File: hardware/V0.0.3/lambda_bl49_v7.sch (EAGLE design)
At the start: 58 parts, among them IC10 MCP2551-E/SN, IC3 LMV321IDBVR, IC4 TLS115B0EJXUMA1, IC6 TLE4270-2D, IC9 CJ125_32, Q3 ABM3-16.000MHZ-D2Y-T

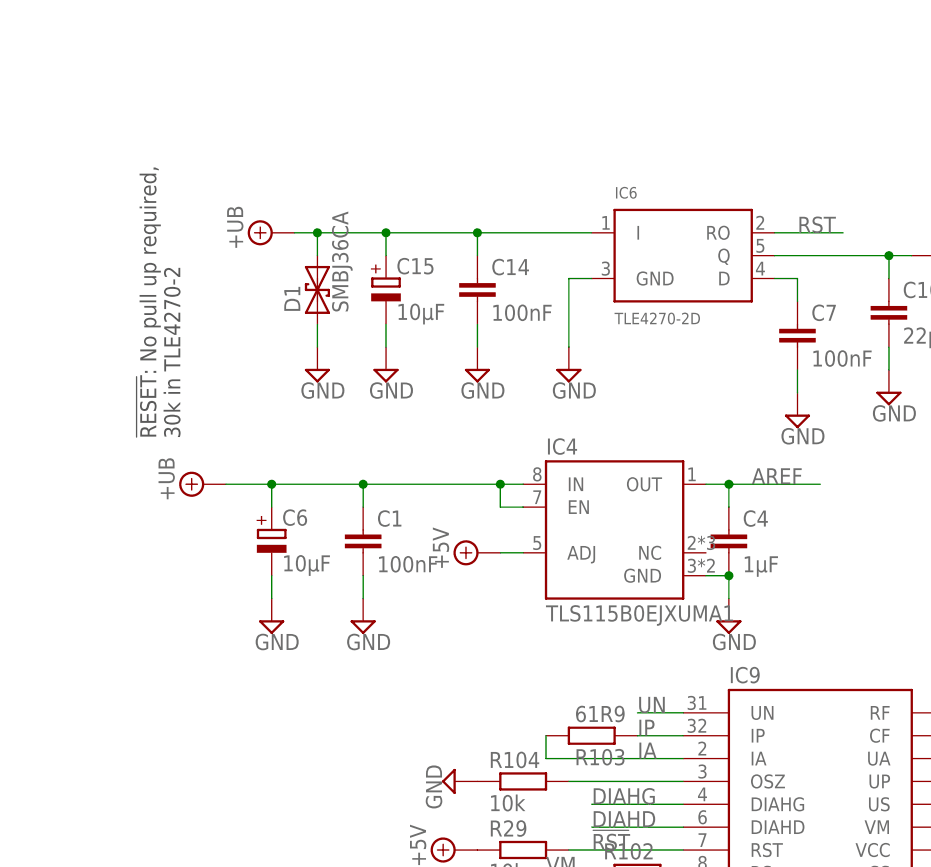
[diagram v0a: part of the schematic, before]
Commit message: tls115 replaced by ti ref5050
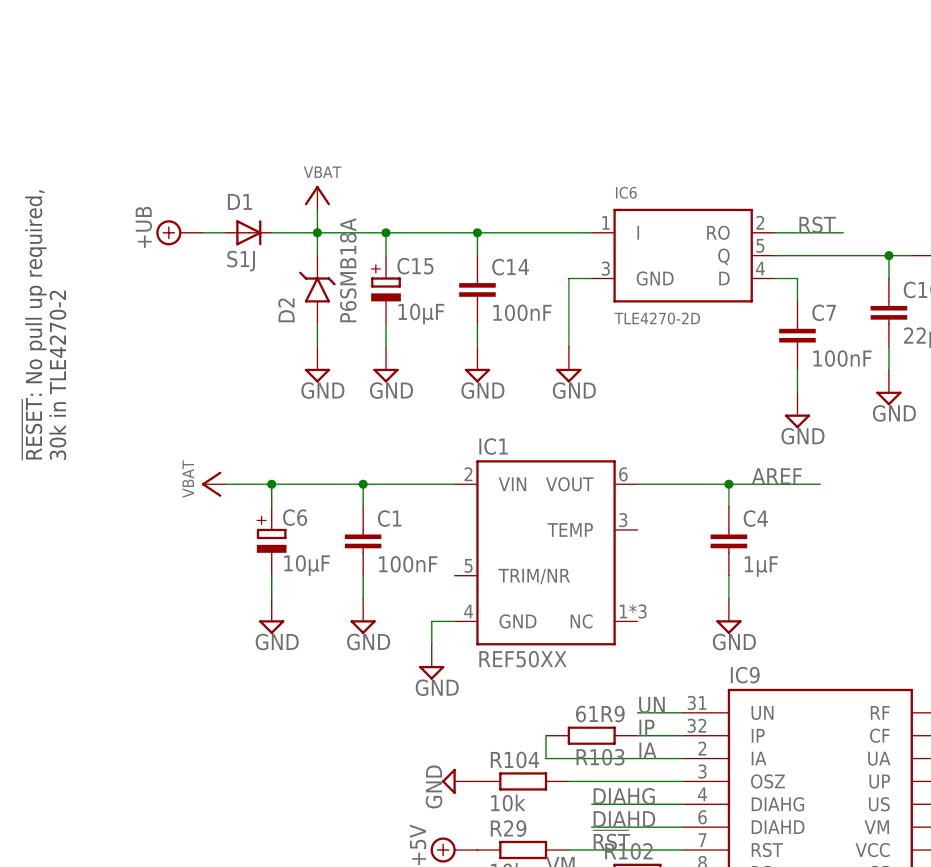
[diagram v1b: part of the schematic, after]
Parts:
- removed IC4: TLS115B0EJXUMA1, Heinrich:TLS115B0EJXUMA1
- added D2: P6SMB18A, Heinrich:P6SMBXXASMB
- added IC1: REF50XX, Heinrich:REF50XX
- D1: value SMBJ36CA -> S1J; device Heinrich:P6SMBXXCA -> Heinrich:DIODESMA
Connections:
- new net VBAT: C1.1, C14.1, C15.+, C6.+, D1.C, D2.C, IC1.VIN, IC6.I
- net +5V: no longer IC4.ADJ
- net +UB: now also D1.A; no longer C1.1, C14.1, C15.+, C6.+, D1.2, IC4.EN, IC4.IN, IC6.I
- net AREF: now also IC1.VOUT; no longer IC4.OUT
- net GND: now also D2.A, IC1.GND; no longer D1.1, IC4.GND
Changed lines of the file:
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@@
 <part name="SUPPLY11" library="supply2" deviceset="+12V" device=""/>
 <part name="SUPPLY6" library="supply2" deviceset="+12V" device=""/>
-<part name="IC4" library="Heinrich" deviceset="TLS115B0EJXUMA1" device=""/>
 <part name="U$12" library="supply2@1" deviceset="GND" device=""/>
 <part name="C4" library="rcl@1" deviceset="C-EU" device="C0603" value="1µF"/>
@@
 <part name="U$13" library="supply2@1" deviceset="GND" device=""/>
 <part name="U$14" library="supply2@1" deviceset="GND" device=""/>
-<part name="D1" library="Heinrich" deviceset="P6SMBXXCA" device="" value="SMBJ36CA"/>
 <part name="C14" library="rcl@1" deviceset="C-EU" device="C0603" value="100nF"/>
 <part name="C15" library="rcl@1" deviceset="CPOL-EU" device="D" value="10µF"/>
@@
 <part name="SUPPLY16" library="supply2@1" deviceset="GND" device=""/>
 <part name="C8" library="rcl@1" deviceset="C-EU" device="C0603" value="100nF"/>
-<part name="SUPPLY17" library="supply2@1" deviceset="+UB" device=""/>
 <part name="SUPPLY18" library="supply2@1" deviceset="GND" device=""/>
 <part name="SUPPLY20" library="supply2@1" deviceset="GND" device=""/>
@@
 <part name="SUPPLY19" library="supply2@1" deviceset="GND" device=""/>
 <part name="SUPPLY22" library="supply2@1" deviceset="GND" device=""/>
-<part name="SUPPLY3" library="supply2@1" deviceset="+5V" device=""/>
+<part name="IC1" library="Heinrich" deviceset="REF50XX" device=""/>
+<part name="SUPPLY3" library="supply2@1" deviceset="GND" device=""/>
+<part name="D2" library="Heinrich" deviceset="P6SMBXXA" device="SMB" value="P6SMB18A"/>
+<part name="D1" library="Heinrich" deviceset="DIODE" device="SMA" value="S1J"/>
+<part name="U$4" library="microbuilder" deviceset="VBAT" device=""/>
+<part name="U$5" library="microbuilder" deviceset="VBAT" device=""/>
 </parts>
 <sheets>
@@
 <text x="227.076" y="167.64" size="1.778" layer="95">1.</text>
 <text x="227.076" y="154.94" size="1.778" layer="95">6.</text>
-<text x="10.16" y="144.78" size="1.778" layer="97" rot="R90">!RESET!: No pull up required,
+<text x="-2.54" y="142.24" size="1.778" layer="97" rot="R90">!RESET!: No pull up required,
 30k in TLE4270-2</text>
 </plain>
@@
 <instance part="LED1" gate="G$1" x="114.3" y="154.94"/>
 <instance part="SUPPLY1" gate="+5V" x="114.3" y="162.56"/>
-<instance part="SUPPLY5" gate="G$1" x="20.32" y="167.64" rot="R90"/>
+<instance part="SUPPLY5" gate="G$1" x="10.16" y="167.64" rot="R90"/>
 <instance part="IC3" gate="G$1" x="139.7" y="33.02"/>
 <instance part="R5" gate="G$1" x="119.38" y="35.56" rot="R180"/>
@@
 <instance part="SUPPLY11" gate="+12V" x="182.88" y="162.56" rot="R270"/>
 <instance part="SUPPLY6" gate="+12V" x="91.44" y="38.1"/>
-<instance part="IC4" gate="G$1" x="58.42" y="134.62"/>
 <instance part="U$12" gate="GND" x="71.12" y="124.46"/>
 <instance part="C4" gate="G$1" x="71.12" y="134.62"/>
@@
 <instance part="U$13" gate="GND" x="20.32" y="124.46"/>
 <instance part="U$14" gate="GND" x="30.48" y="124.46"/>
-<instance part="D1" gate="G$1" x="25.4" y="160.02" rot="R90"/>
 <instance part="C14" gate="G$1" x="43.18" y="162.56"/>
 <instance part="C15" gate="G$1" x="33.02" y="162.56"/>
@@
 <instance part="SUPPLY16" gate="GND" x="53.34" y="152.4"/>
 <instance part="C8" gate="G$1" x="55.88" y="78.74"/>
-<instance part="SUPPLY17" gate="G$1" x="12.7" y="139.7" rot="R90"/>
 <instance part="SUPPLY18" gate="GND" x="226.06" y="99.06"/>
 <instance part="SUPPLY20" gate="GND" x="114.3" y="134.62"/>
@@
 <instance part="SUPPLY19" gate="GND" x="208.28" y="58.42"/>
 <instance part="SUPPLY22" gate="GND" x="218.44" y="58.42"/>
-<instance part="SUPPLY3" gate="+5V" x="43.18" y="132.08" rot="R90"/>
+<instance part="IC1" gate="G$1" x="50.8" y="132.08"/>
+<instance part="SUPPLY3" gate="GND" x="38.1" y="119.38"/>
+<instance part="D2" gate="G$1" x="25.4" y="162.56" rot="R90"/>
+<instance part="D1" gate="G$1" x="17.78" y="167.64"/>
+<instance part="U$4" gate="G$1" x="25.4" y="170.18"/>
+<instance part="U$5" gate="G$1" x="15.24" y="139.7" rot="R90"/>
 </instances>
 <busses>
@@
 </segment>
 <segment>
-<pinref part="IC4" gate="G$1" pin="GND"/>
-<wire x1="68.58" y1="129.54" x2="71.12" y2="129.54" width="0.1524" layer="91"/>
 <pinref part="U$12" gate="GND" pin="GND"/>
 <wire x1="71.12" y1="129.54" x2="71.12" y2="127" width="0.1524" layer="91"/>
 <pinref part="C4" gate="G$1" pin="2"/>
-<junction x="71.12" y="129.54"/>
 </segment>
 <segment>
@@
 </segment>
 <segment>
-<pinref part="D1" gate="G$1" pin="1"/>
 <wire x1="25.4" y1="157.48" x2="25.4" y2="154.94" width="0.1524" layer="91"/>
 <pinref part="SUPPLY13" gate="GND" pin="GND"/>
+<pinref part="D2" gate="G$1" pin="A"/>
 </segment>
 <segment>
@@
 <pinref part="SUPPLY22" gate="GND" pin="GND"/>
 </segment>
+<segment>
+<pinref part="IC1" gate="G$1" pin="GND"/>
+<wire x1="40.64" y1="124.46" x2="38.1" y2="124.46" width="0.1524" layer="91"/>
+<wire x1="38.1" y1="124.46" x2="38.1" y2="121.92" width="0.1524" layer="91"/>
+<pinref part="SUPPLY3" gate="GND" pin="GND"/>
+</segment>
 </net>
 <net name="+5V" class="0">
@@
 <wire x1="88.9" y1="162.56" x2="88.9" y2="165.1" width="0.1524" layer="91"/>
 <junction x="88.9" y="165.1"/>
-</segment>
-<segment>
-<pinref part="IC4" gate="G$1" pin="ADJ"/>
-<wire x1="48.26" y1="132.08" x2="45.72" y2="132.08" width="0.1524" layer="91"/>
-<pinref part="SUPPLY3" gate="+5V" pin="+5V"/>
 </segment>
 </net>
@@
 </segment>
 <segment>
-<pinref part="D1" gate="G$1" pin="2"/>
-<wire x1="25.4" y1="165.1" x2="25.4" y2="167.64" width="0.1524" layer="91"/>
-<wire x1="25.4" y1="167.64" x2="22.86" y2="167.64" width="0.1524" layer="91"/>
-<wire x1="25.4" y1="167.64" x2="33.02" y2="167.64" width="0.1524" layer="91"/>
-<junction x="25.4" y="167.64"/>
-<pinref part="C15" gate="G$1" pin="+"/>
-<wire x1="33.02" y1="165.1" x2="33.02" y2="167.64" width="0.1524" layer="91"/>
-<wire x1="33.02" y1="167.64" x2="43.18" y2="167.64" width="0.1524" layer="91"/>
-<junction x="33.02" y="167.64"/>
-<pinref part="C14" gate="G$1" pin="1"/>
-<wire x1="43.18" y1="167.64" x2="55.88" y2="167.64" width="0.1524" layer="91"/>
-<wire x1="43.18" y1="165.1" x2="43.18" y2="167.64" width="0.1524" layer="91"/>
-<junction x="43.18" y="167.64"/>
-<pinref part="IC6" gate="G$1" pin="I"/>
+<pinref part="D1" gate="G$1" pin="A"/>
 <pinref part="SUPPLY5" gate="G$1" pin="+UB"/>
-</segment>
-<segment>
-<pinref part="IC4" gate="G$1" pin="IN"/>
-<wire x1="48.26" y1="139.7" x2="45.72" y2="139.7" width="0.1524" layer="91"/>
-<pinref part="IC4" gate="G$1" pin="EN"/>
-<wire x1="45.72" y1="139.7" x2="30.48" y2="139.7" width="0.1524" layer="91"/>
-<wire x1="30.48" y1="139.7" x2="20.32" y2="139.7" width="0.1524" layer="91"/>
-<wire x1="48.26" y1="137.16" x2="45.72" y2="137.16" width="0.1524" layer="91"/>
-<wire x1="45.72" y1="137.16" x2="45.72" y2="139.7" width="0.1524" layer="91"/>
-<junction x="45.72" y="139.7"/>
-<pinref part="C1" gate="G$1" pin="1"/>
-<wire x1="30.48" y1="137.16" x2="30.48" y2="139.7" width="0.1524" layer="91"/>
-<junction x="30.48" y="139.7"/>
-<pinref part="C6" gate="G$1" pin="+"/>
-<wire x1="20.32" y1="137.16" x2="20.32" y2="139.7" width="0.1524" layer="91"/>
-<wire x1="20.32" y1="139.7" x2="15.24" y2="139.7" width="0.1524" layer="91"/>
-<junction x="20.32" y="139.7"/>
-<pinref part="SUPPLY17" gate="G$1" pin="+UB"/>
+<wire x1="15.24" y1="167.64" x2="12.7" y2="167.64" width="0.1524" layer="91"/>
 </segment>
 </net>
@@
 <net name="AREF" class="0">
 <segment>
-<pinref part="IC4" gate="G$1" pin="OUT"/>
-<wire x1="68.58" y1="139.7" x2="71.12" y2="139.7" width="0.1524" layer="91"/>
 <label x="73.66" y="139.7" size="1.778" layer="95"/>
 <pinref part="C4" gate="G$1" pin="1"/>
@@
 <wire x1="71.12" y1="139.7" x2="71.12" y2="137.16" width="0.1524" layer="91"/>
 <junction x="71.12" y="139.7"/>
+<pinref part="IC1" gate="G$1" pin="VOUT"/>
+<wire x1="71.12" y1="139.7" x2="60.96" y2="139.7" width="0.1524" layer="91"/>
 </segment>
 <segment>
@@
 </segment>
 </net>
+<net name="VBAT" class="0">
+<segment>
+<wire x1="25.4" y1="165.1" x2="25.4" y2="167.64" width="0.1524" layer="91"/>
+<wire x1="25.4" y1="167.64" x2="33.02" y2="167.64" width="0.1524" layer="91"/>
+<pinref part="C15" gate="G$1" pin="+"/>
+<wire x1="33.02" y1="165.1" x2="33.02" y2="167.64" width="0.1524" layer="91"/>
+<wire x1="33.02" y1="167.64" x2="43.18" y2="167.64" width="0.1524" layer="91"/>
+<junction x="33.02" y="167.64"/>
+<pinref part="C14" gate="G$1" pin="1"/>
+<wire x1="43.18" y1="167.64" x2="55.88" y2="167.64" width="0.1524" layer="91"/>
+<wire x1="43.18" y1="165.1" x2="43.18" y2="167.64" width="0.1524" layer="91"/>
+<junction x="43.18" y="167.64"/>
+<pinref part="IC6" gate="G$1" pin="I"/>
+<pinref part="D2" gate="G$1" pin="C"/>
+<pinref part="D1" gate="G$1" pin="C"/>
+<wire x1="20.32" y1="167.64" x2="25.4" y2="167.64" width="0.1524" layer="91"/>
+<junction x="25.4" y="167.64"/>
+<pinref part="U$4" gate="G$1" pin="VBAT"/>
+<wire x1="25.4" y1="170.18" x2="25.4" y2="167.64" width="0.1524" layer="91"/>
+</segment>
+<segment>
+<wire x1="30.48" y1="139.7" x2="20.32" y2="139.7" width="0.1524" layer="91"/>
+<pinref part="C1" gate="G$1" pin="1"/>
+<wire x1="30.48" y1="137.16" x2="30.48" y2="139.7" width="0.1524" layer="91"/>
+<pinref part="C6" gate="G$1" pin="+"/>
+<wire x1="20.32" y1="137.16" x2="20.32" y2="139.7" width="0.1524" layer="91"/>
+<wire x1="20.32" y1="139.7" x2="15.24" y2="139.7" width="0.1524" layer="91"/>
+<junction x="20.32" y="139.7"/>
+<wire x1="30.48" y1="139.7" x2="40.64" y2="139.7" width="0.1524" layer="91"/>
+<junction x="30.48" y="139.7"/>
+<pinref part="IC1" gate="G$1" pin="VIN"/>
+<pinref part="U$5" gate="G$1" pin="VBAT"/>
+</segment>
+</net>
